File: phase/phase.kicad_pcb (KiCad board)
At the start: 2 copper layers, 128 x 92.6 mm, 72 parts, among them J1 USB_C_Receptacle_USB2.0, J2 AudioJack4, K1 KEYSW, K10 KEYSW, K11 KEYSW, K12 KEYSW, K13 KEYSW, K14 KEYSW, K15 KEYSW, K16 KEYSW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

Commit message: renamed files to remove version number, add gitignore
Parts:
- D1, D10, D11, D12, D13, D14, D15, D16, D17, D18, D19, D2, D20, D21, D3, D4, D5, D6, D7, D8, D9: footprint phase_v1_0:D_SOD-123-dual -> phase:D_SOD-123-dual
- G***: footprint phase_v1_0:squares160 -> phase:squares160
- G***: footprint phase_v1_0:circles160 -> phase:circles160
- J2: footprint phase_v1_0:TRRS-PJ-320A-dual -> phase:TRRS-PJ-320A-dual
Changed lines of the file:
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@@
       (drillshape 0)
       (scaleselection 1)
-      (outputdirectory "/Users/matthewpauly/Documents/KiCad/phase_v1_0/gerbers/"))
+      (outputdirectory "/Users/matthewpauly/Documents/KiCad/phase/gerbers/"))
   )
   (net 0 "")
@@
     (pad 1 np_thru_hole circle (at 0 0) (size 2.7 2.7) (drill 2.7) (layers *.Cu *.Mask))
   )
-  (module phase_v1_0:squares160 (layer B.Cu)
+  (module phase:squares160 (layer B.Cu)
     (at 107 73.75 180)
     (fp_text reference G*** (at 0 0) (layer B.SilkS) hide
@@
       (xy -64.417222 -59.760556) (xy -63.006111 -59.760556) (xy -63.006111 -63.006111)) (layer B.SilkS) (width 0.01))
   )
-  (module phase_v1_0:circles160 (layer F.Cu)
+  (module phase:circles160 (layer F.Cu)
     (at 107 73.75 180)
     (fp_text reference G*** (at 0 0) (layer F.SilkS) hide
@@
     )
   )
-  (module phase_v1_0:TRRS-PJ-320A-dual (layer F.Cu)
+  (module phase:TRRS-PJ-320A-dual (layer F.Cu)
     (at 169.164 103.124 270)
     (fp_text reference J2 (at 0 14.2 90) (layer Dwgs.User)
@@
     )
   )
-  (module phase_v1_0:D_SOD-123-dual (layer F.Cu)
+  (module phase:D_SOD-123-dual (layer F.Cu)
     (at 59.5 76.6 90)
     (descr SOD-123)
@@
     )
   )
-  (module phase_v1_0:D_SOD-123-dual (layer F.Cu)
+  (module phase:D_SOD-123-dual (layer F.Cu)
     (at 59.5 95.6 90)
     (descr SOD-123)
@@
     )
   )
-  (module phase_v1_0:D_SOD-123-dual (layer F.Cu)
+  (module phase:D_SOD-123-dual (layer F.Cu)
     (at 59.5 114.6 90)
     (descr SOD-123)
@@
     )
   )
-  (module phase_v1_0:D_SOD-123-dual (layer F.Cu)
+  (module phase:D_SOD-123-dual (layer F.Cu)
     (at 78.5 76.6 90)
     (descr SOD-123)
@@
     )
   )
-  (module phase_v1_0:D_SOD-123-dual (layer F.Cu)
+  (module phase:D_SOD-123-dual (layer F.Cu)
     (at 78.5 95.6 90)
     (descr SOD-123)
@@
     )
   )
-  (module phase_v1_0:D_SOD-123-dual (layer F.Cu)
+  (module phase:D_SOD-123-dual (layer F.Cu)
     (at 78.5 114.6 90)
     (descr SOD-123)
@@
     )
   )
-  (module phase_v1_0:D_SOD-123-dual (layer F.Cu)
+  (module phase:D_SOD-123-dual (layer F.Cu)
     (at 97.5 67.1 90)
     (descr SOD-123)
@@
     )
   )
-  (module phase_v1_0:D_SOD-123-dual (layer F.Cu)
+  (module phase:D_SOD-123-dual (layer F.Cu)
     (at 97.5 86.1 90)
     (descr SOD-123)
@@
     )
   )
-  (module phase_v1_0:D_SOD-123-dual (layer F.Cu)
+  (module phase:D_SOD-123-dual (layer F.Cu)
     (at 97.5 105.1 90)
     (descr SOD-123)
@@
     )
   )
-  (module phase_v1_0:D_SOD-123-dual (layer F.Cu)
+  (module phase:D_SOD-123-dual (layer F.Cu)
     (at 116.5 62.35 90)
     (descr SOD-123)
@@
     )
   )
-  (module phase_v1_0:D_SOD-123-dual (layer F.Cu)
+  (module phase:D_SOD-123-dual (layer F.Cu)
     (at 116.5 81.35 90)
     (descr SOD-123)
@@
     )
   )
-  (module phase_v1_0:D_SOD-123-dual (layer F.Cu)
+  (module phase:D_SOD-123-dual (layer F.Cu)
     (at 116.5 100.35 90)
     (descr SOD-123)
@@
     )
   )
-  (module phase_v1_0:D_SOD-123-dual (layer F.Cu)
+  (module phase:D_SOD-123-dual (layer F.Cu)
     (at 126 124.1 90)
     (descr SOD-123)
@@
     )
   )
-  (module phase_v1_0:D_SOD-123-dual (layer F.Cu)
+  (module phase:D_SOD-123-dual (layer F.Cu)
     (at 135.5 67.1 90)
     (descr SOD-123)
@@
     )
   )
-  (module phase_v1_0:D_SOD-123-dual (layer F.Cu)
+  (module phase:D_SOD-123-dual (layer F.Cu)
     (at 135.5 86.1 90)
     (descr SOD-123)
@@
     )
   )
-  (module phase_v1_0:D_SOD-123-dual (layer F.Cu)
+  (module phase:D_SOD-123-dual (layer F.Cu)
     (at 135.5 105.1 90)
     (descr SOD-123)
@@
     )
   )
-  (module phase_v1_0:D_SOD-123-dual (layer F.Cu)
+  (module phase:D_SOD-123-dual (layer F.Cu)
     (at 144.24 129.003 75)
     (descr SOD-123)
@@
     )
   )
-  (module phase_v1_0:D_SOD-123-dual (layer F.Cu)
+  (module phase:D_SOD-123-dual (layer F.Cu)
     (at 154.5 69.475 90)
     (descr SOD-123)
@@
     )
   )
-  (module phase_v1_0:D_SOD-123-dual (layer F.Cu)
+  (module phase:D_SOD-123-dual (layer F.Cu)
     (at 154.5 88.475 90)
     (descr SOD-123)
@@
     )
   )
-  (module phase_v1_0:D_SOD-123-dual (layer F.Cu)
+  (module phase:D_SOD-123-dual (layer F.Cu)
     (at 154.5 107.475 90)
     (descr SOD-123)
@@
     )
   )
-  (module phase_v1_0:D_SOD-123-dual (layer F.Cu)
+  (module phase:D_SOD-123-dual (layer F.Cu)
     (at 162.965 134.346 60)
     (descr SOD-123)

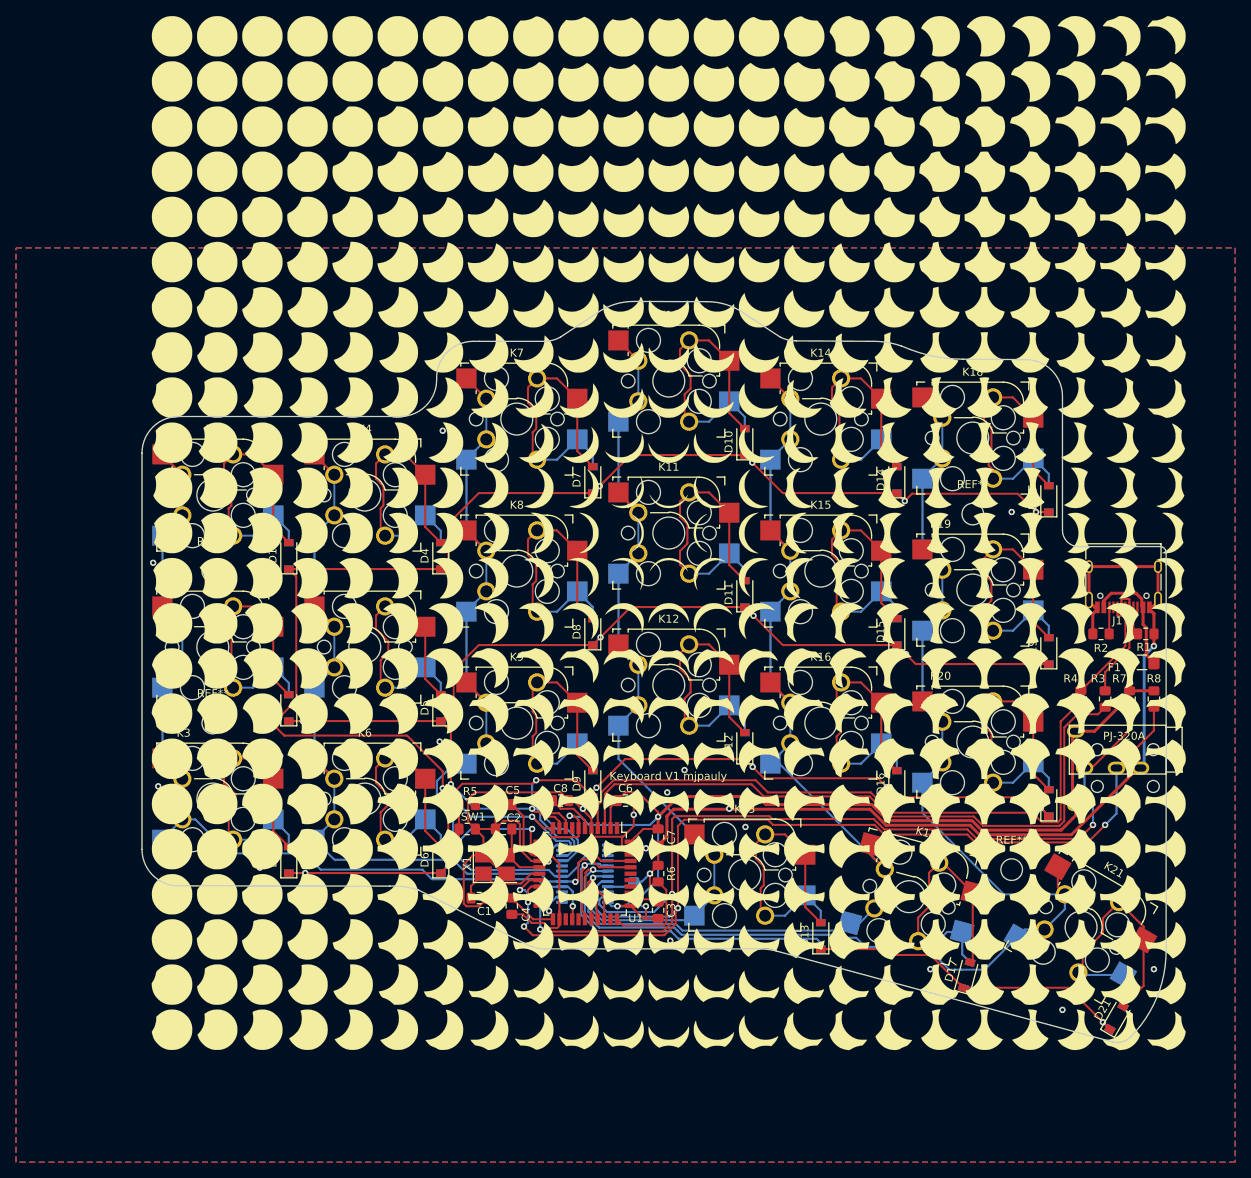
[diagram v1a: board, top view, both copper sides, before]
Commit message: fix sda/scl swap, remove silkscreen art and unneeded ref des
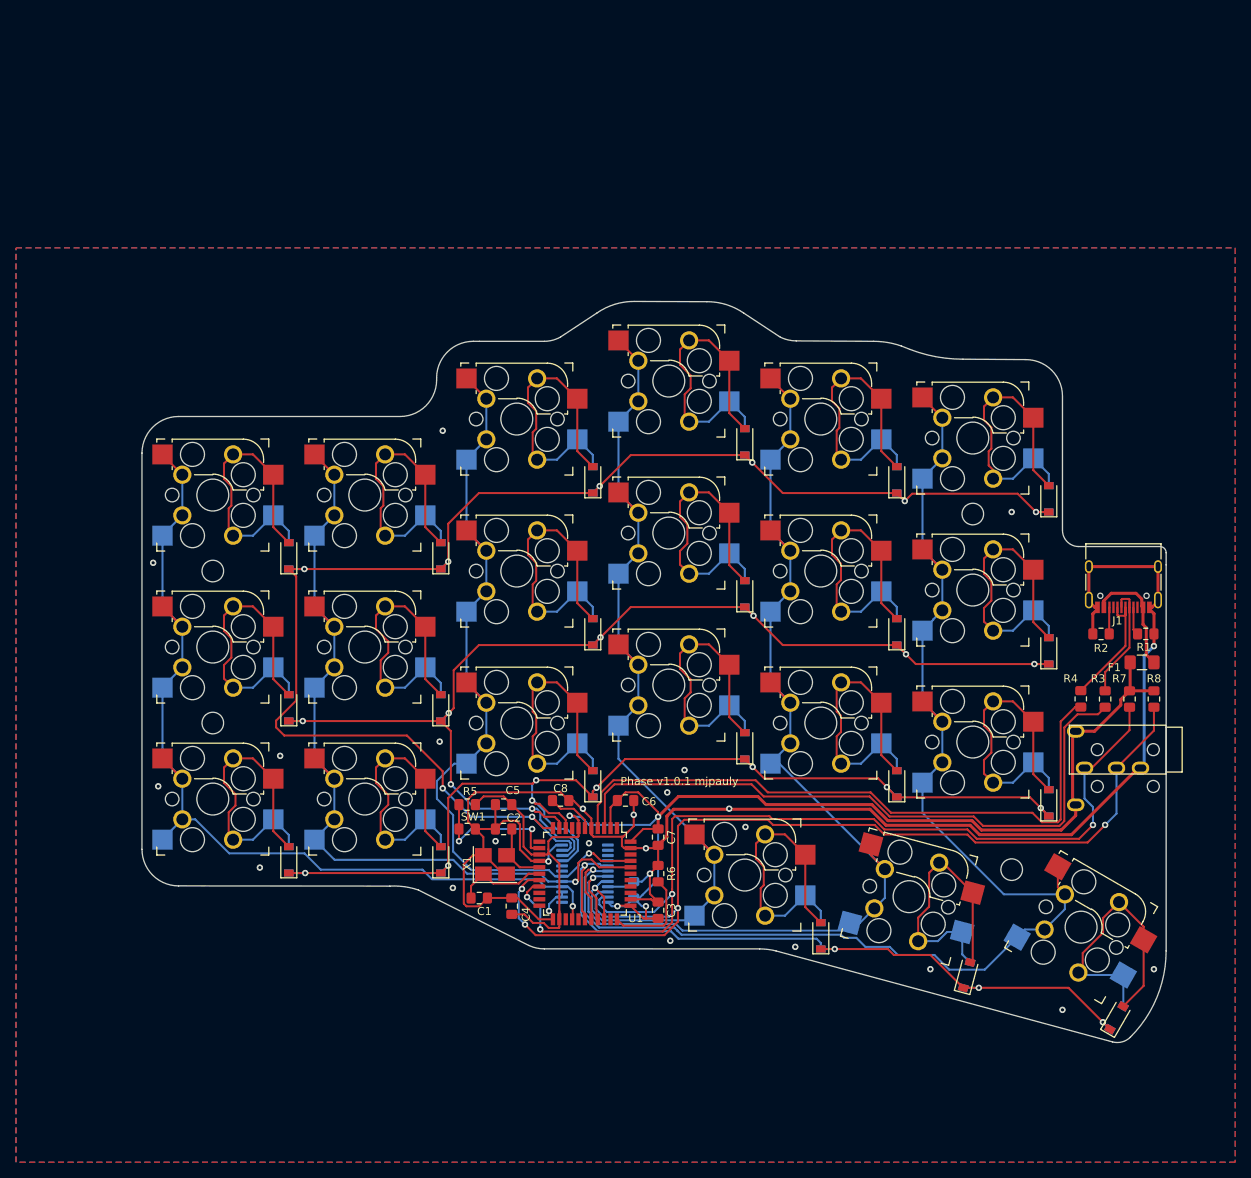
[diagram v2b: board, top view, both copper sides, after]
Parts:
- removed G***: LOGO, phase:squares160
- removed G***: LOGO, phase:circles160
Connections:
- U1 pad 18: /SDA -> /SCL
- U1 pad 19: /SCL -> /SDA
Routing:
- net /SDA: track 124.1 -> 122.3 mm
- net /SCL: track 126.4 -> 127.6 mm
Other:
- board text added: "Phase v1.0.1 mjpauly"
- board text removed: "Keyboard V1 mjpauly"
